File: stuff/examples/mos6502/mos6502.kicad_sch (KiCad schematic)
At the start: 16 parts

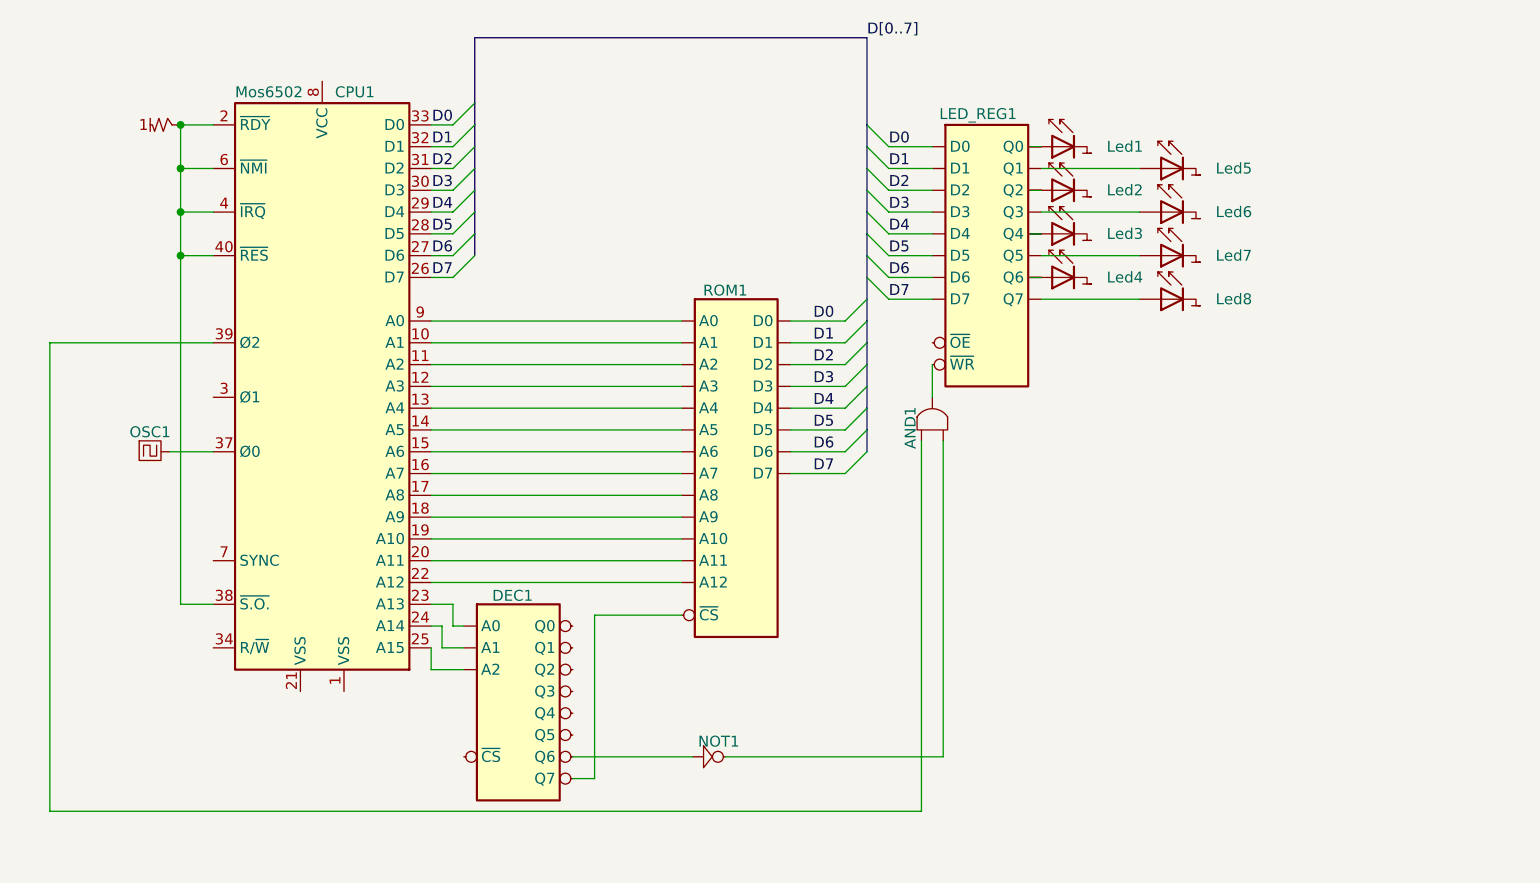
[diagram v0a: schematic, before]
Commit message: Mos6502 - fix logic.
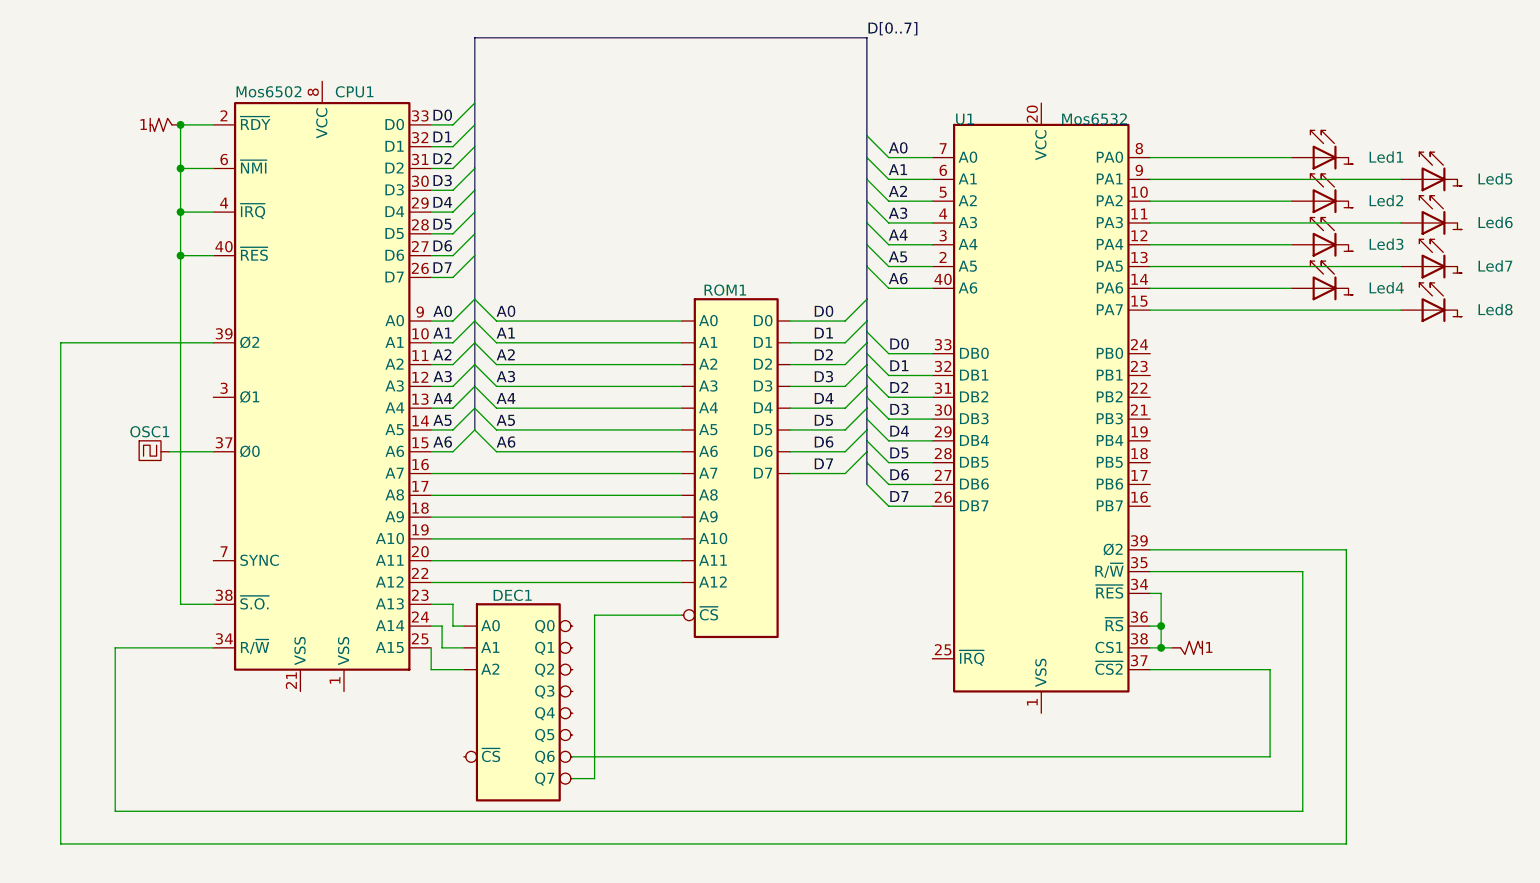
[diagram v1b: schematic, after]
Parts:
- removed AND1: AND, symbol chip:AND
- removed LED_REG1: LED_REG, symbol chip:8REG
- removed NOT1: NOT, symbol chip:NOT
- added U1: Mos6532, Package_DIP:DIP-40_W15.24mm, symbol retro:Mos6532
- added pullup2: pull_up, symbol chip:PULLUP
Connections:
- net D0: now also U1.33 (DB0)
- net D1: now also U1.32 (DB1)
- net D2: now also U1.31 (DB2)
- net D3: now also U1.30 (DB3)
- net D4: now also U1.29 (DB4)
- net D5: now also U1.28 (DB5)
- net D6: now also U1.27 (DB6)
- net D7: now also U1.26 (DB7)
- net at DEC1.10 (Q6): now also U1.37 (~{CS2})
- net at Led2.1 (IN): now also U1.10 (PA2)
- net at Led8.1 (IN): now also U1.15 (PA7)
- net at CPU1.39 (Ø2): now also U1.39 (Ø2)
- net at Led4.1 (IN): now also U1.14 (PA6)
- net at Led5.1 (IN): now also U1.9 (PA1)
- net at Led6.1 (IN): now also U1.11 (PA3)
- net at Led3.1 (IN): now also U1.12 (PA4)
- net A1: now reaches CPU1.10 (A1), ROM1.2 (A1)
- net A1: now also U1.6 (A1)
- net A2: now reaches CPU1.11 (A2), ROM1.6 (A2)
- net A2: now also U1.5 (A2)
- net A3: now reaches CPU1.12 (A3), ROM1.7 (A3)
- net A3: now also U1.4 (A3)
- net A4: now reaches CPU1.13 (A4), ROM1.8 (A4)
- net A4: now also U1.3 (A4)
- net A5: now reaches CPU1.14 (A5), ROM1.9 (A5)
- net A5: now also U1.2 (A5)
- net A6: now reaches CPU1.15 (A6), ROM1.10 (A6)
- net A6: now also U1.40 (A6)
- net at CPU1.34 (R/~{W}): now also U1.35 (R/~{W})
- net A0: now reaches CPU1.9 (A0), ROM1.1 (A0)
- net A0: now also U1.7 (A0)
- net at Led7.1 (IN): now also U1.13 (PA5)
- net at Led1.1 (IN): now also U1.8 (PA0)
- new net: U1.34 (~{RES}), U1.36 (~{RS}), U1.38 (CS1), pullup2.1 (OUT)
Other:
- moved on the sheet: Led1, Led2, Led3, Led4, Led5, Led6, Led7, Led8

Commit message: Mos6502/6532 - example
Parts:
- added AND1: AND, symbol chip:AND
- added pullup3: pull_up, symbol chip:PULLUP
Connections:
- net at Led2.1 (IN): now also U1.22 (PB2); no longer U1.10 (PA2)
- net at Led8.1 (IN): now also U1.16 (PB7); no longer U1.15 (PA7)
- net at U1.34 (~{RES}), U1.38 (CS1), pullup2.1 (OUT): no longer U1.36 (~{RS})
- net at CPU1.2 (~{RDY}), CPU1.38 (~{S.O.}), CPU1.4 (~{IRQ})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: no longer CPU1.6 (~{NMI})
- net at Led4.1 (IN): now also U1.17 (PB6); no longer U1.14 (PA6)
- net at Led5.1 (IN): now also U1.23 (PB1); no longer U1.9 (PA1)
- net at Led6.1 (IN): now also U1.21 (PB3); no longer U1.11 (PA3)
- net at DEC1.10 (Q6): now also AND1.2 (IN1); no longer U1.37 (~{CS2})
- net at DEC1.4 (Q0): now also U1.36 (~{RS}), AND1.1 (IN0)
- net at Led3.1 (IN): now also U1.19 (PB4); no longer U1.12 (PA4)
- net at Led7.1 (IN): now also U1.18 (PB5); no longer U1.13 (PA5)
- net at U1.24 (PB0): now also Led1.1 (IN)
- net at U1.25 (~{IRQ}): now also CPU1.6 (~{NMI}), pullup3.1 (OUT)
- net at U1.8 (PA0): no longer Led1.1 (IN)
- new net: AND1.3 (OUT), U1.37 (~{CS2})
